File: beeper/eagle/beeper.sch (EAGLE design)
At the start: 32 parts, among them J4 ICSP, Q1 16MHz, T1 MMBT3904, U1 ATA6631, U2 ATMEGA328P

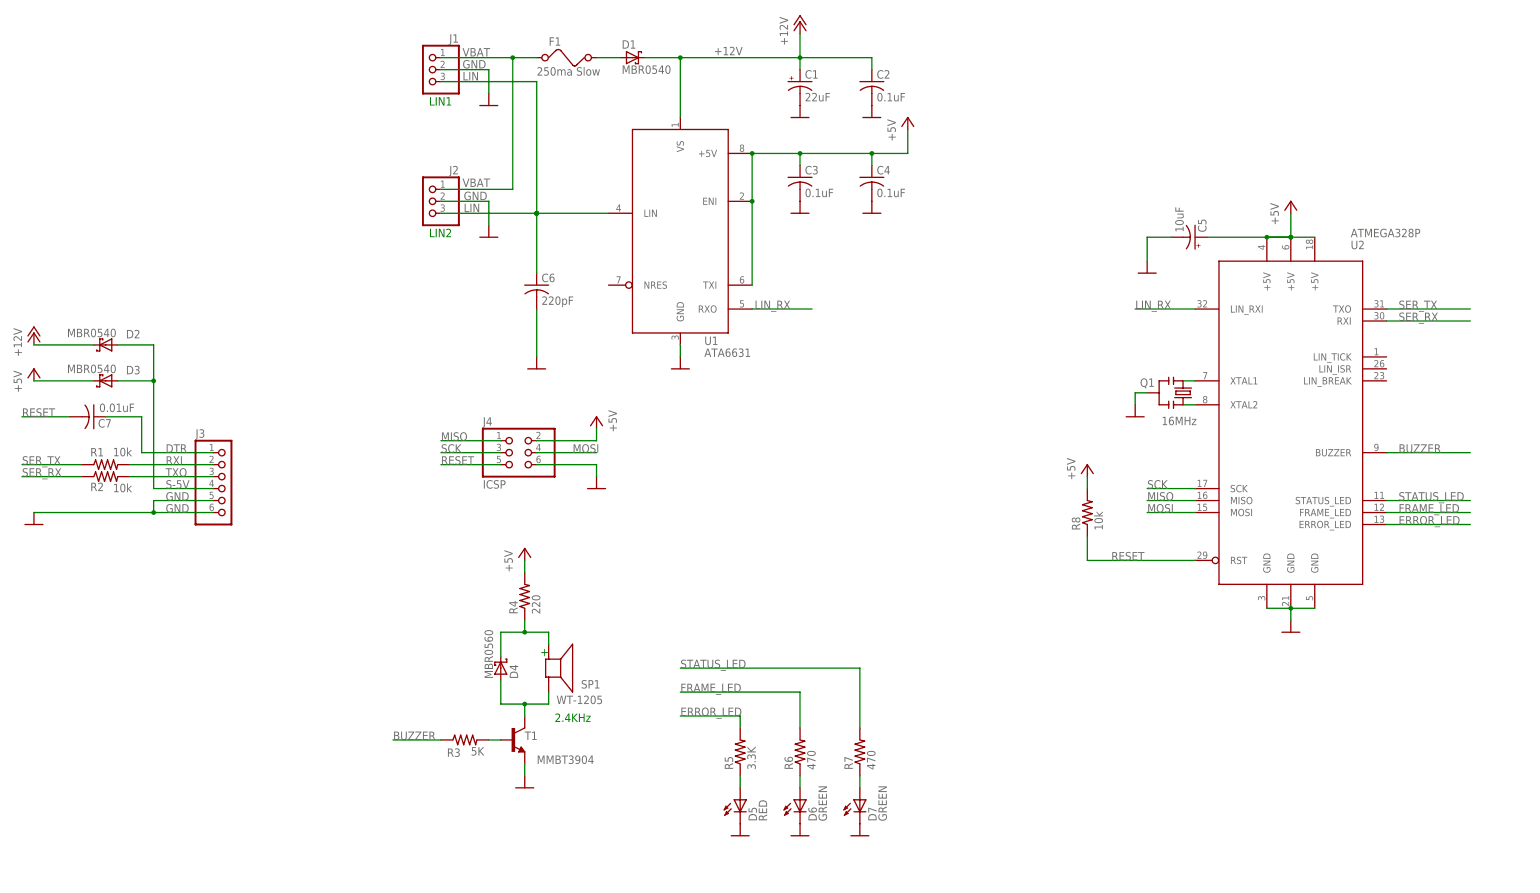
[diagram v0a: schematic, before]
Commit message: Complected the refactoring of the beeper schema. No semantic change.
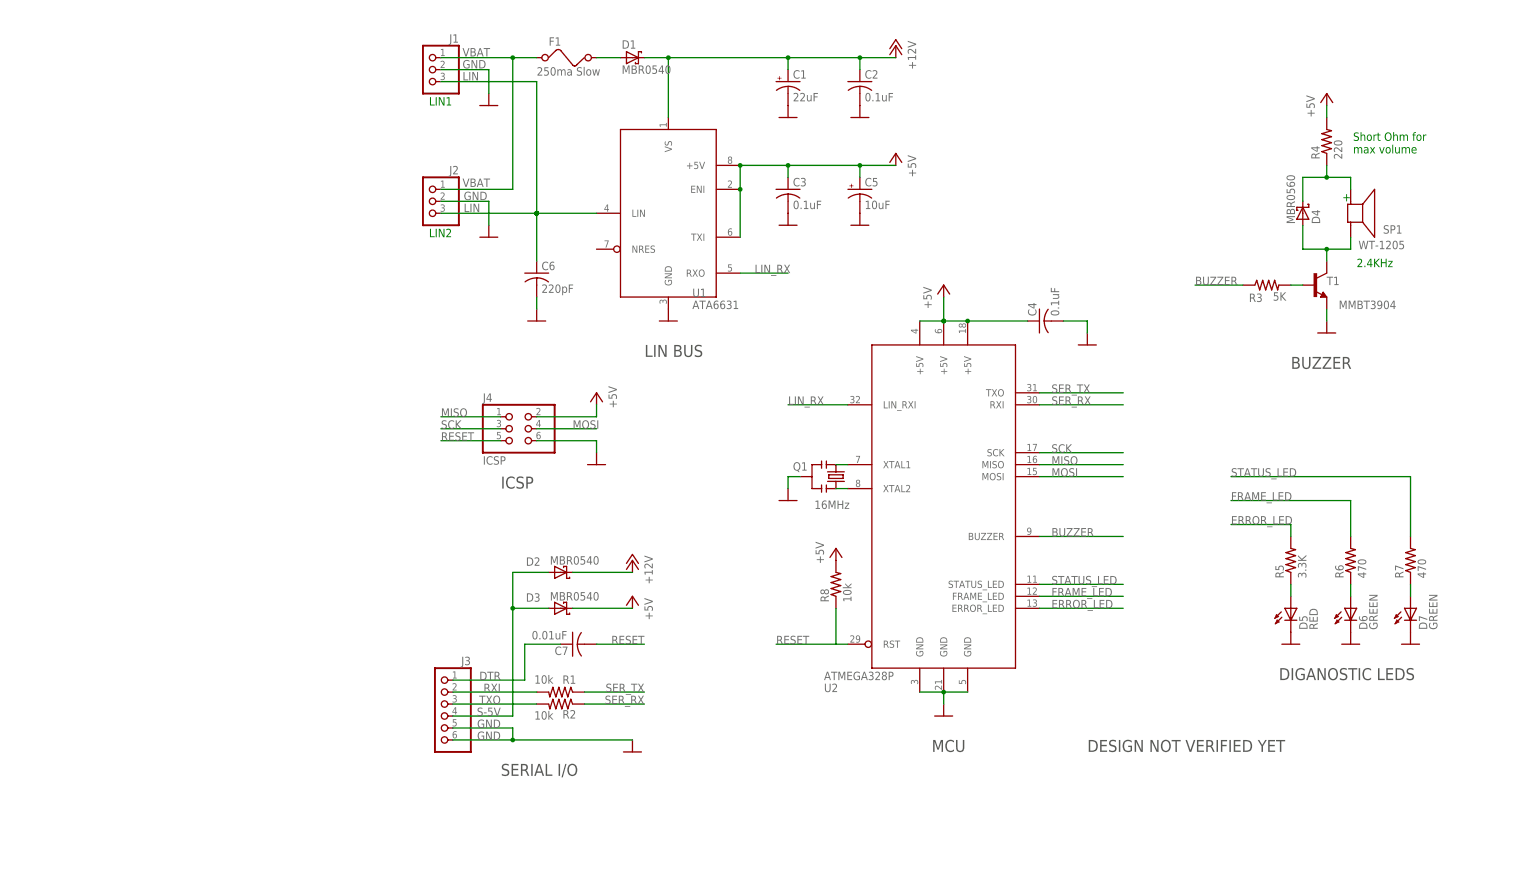
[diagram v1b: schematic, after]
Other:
- note added: "BUZZER"
- note added: "DESIGN NOT VERIFIED YET"
- note added: "DIGANOSTIC LEDS"
- note added: "ICSP"
- note added: "LIN BUS"
- note added: "MCU"
- note added: "SERIAL I/O"
- note added: "Short Ohm for max volume"
- moved on the sheet: C1, C2, C3, C4, C5, C6, C7, D2, D3, D4, D5, D6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

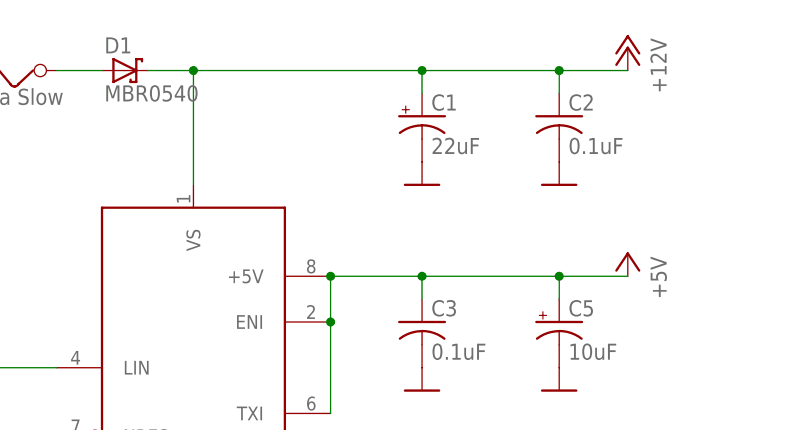
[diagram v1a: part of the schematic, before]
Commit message: Added '40V' annotation to VBAT capacitor.
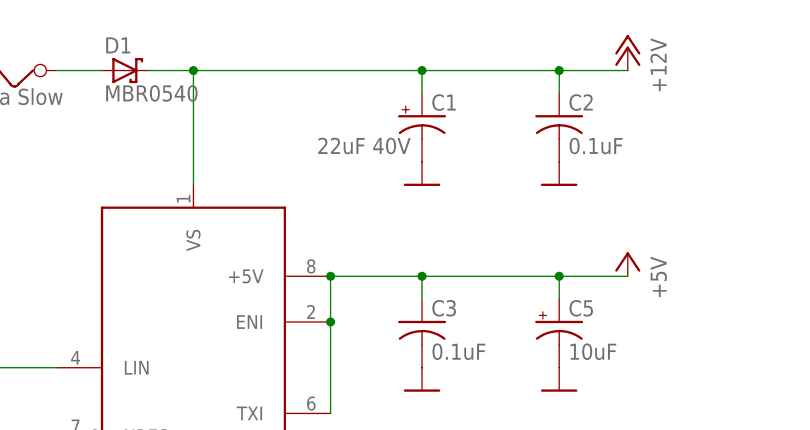
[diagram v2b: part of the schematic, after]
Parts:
- C1: value 22uF -> 22uF 40V
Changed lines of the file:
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@@
 <part name="D6" library="led" deviceset="LED" device="SMT1206" value="GREEN"/>
 <part name="D7" library="led" deviceset="LED" device="SMT1206" value="GREEN"/>
-<part name="C1" library="rcl" deviceset="CPOL-US" device="UD-6,3X5,8" value="22uF"/>
+<part name="C1" library="rcl" deviceset="CPOL-US" device="UD-6,3X5,8" value="22uF 40V"/>
 <part name="C2" library="rcl" deviceset="C-US" device="C0805" value="0.1uF"/>
 <part name="C5" library="rcl" deviceset="CPOL-US" device="A/3216-18R" value="10uF"/>
@@
 <instance part="D6" gate="G$1" x="271.78" y="83.82"/>
 <instance part="D7" gate="G$1" x="284.48" y="83.82"/>
-<instance part="C1" gate="G$1" x="152.4" y="195.58"/>
+<instance part="C1" gate="G$1" x="152.4" y="195.58" smashed="yes">
+<attribute name="NAME" x="153.416" y="196.215" size="1.778" layer="95"/>
+<attribute name="VALUE" x="140.716" y="191.389" size="1.778" layer="96"/>
+</instance>
 <instance part="C2" gate="G$1" x="167.64" y="195.58"/>
 <instance part="C5" gate="G$1" x="167.64" y="172.72"/>

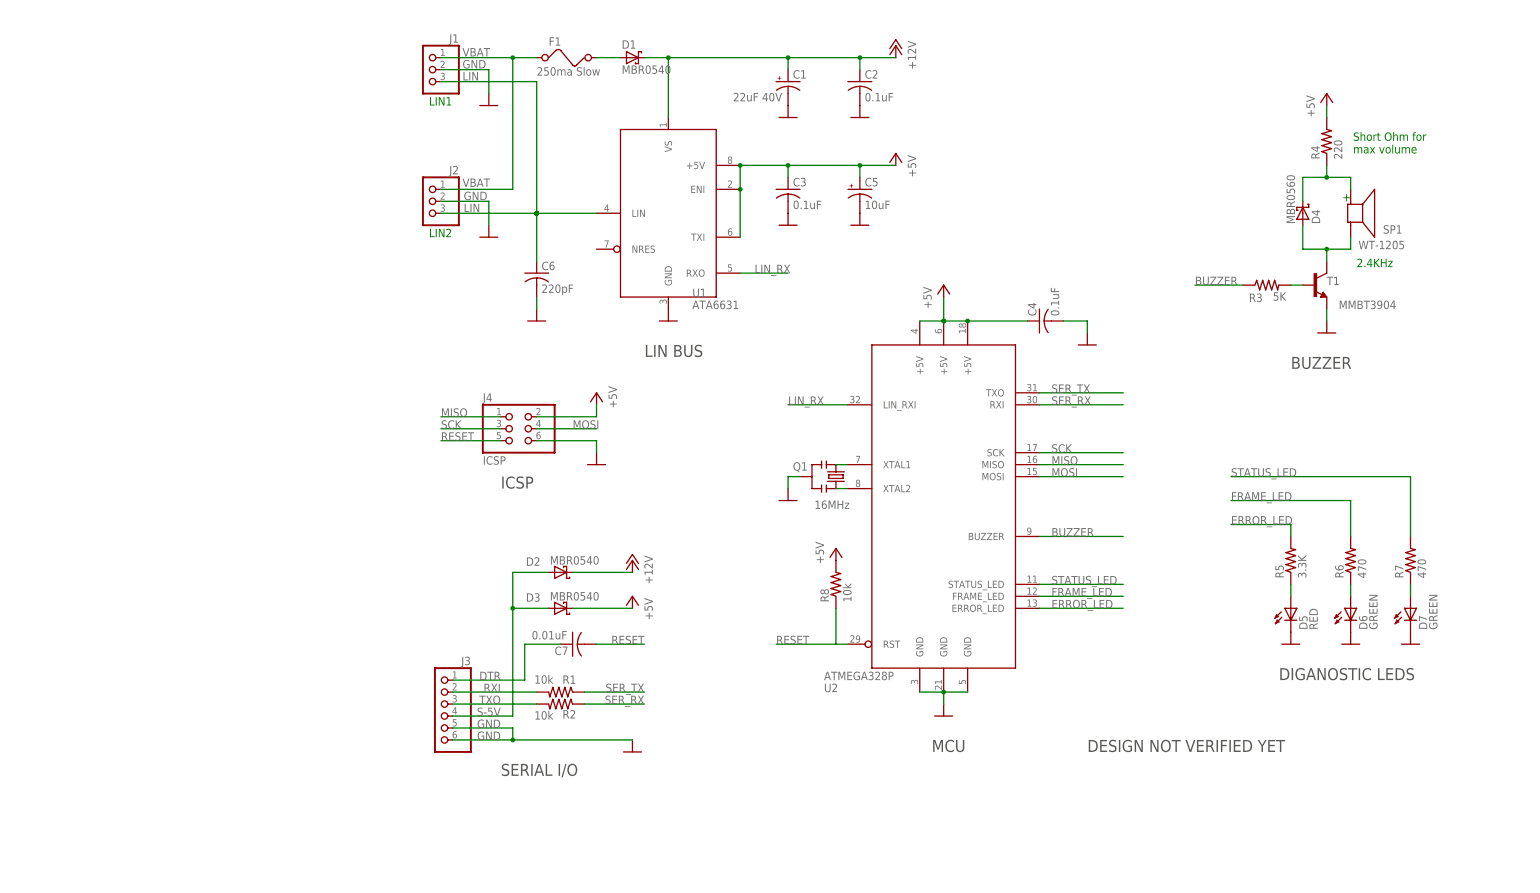
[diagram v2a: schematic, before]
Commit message: Minor text changes in beeper schematic. No semantic change.
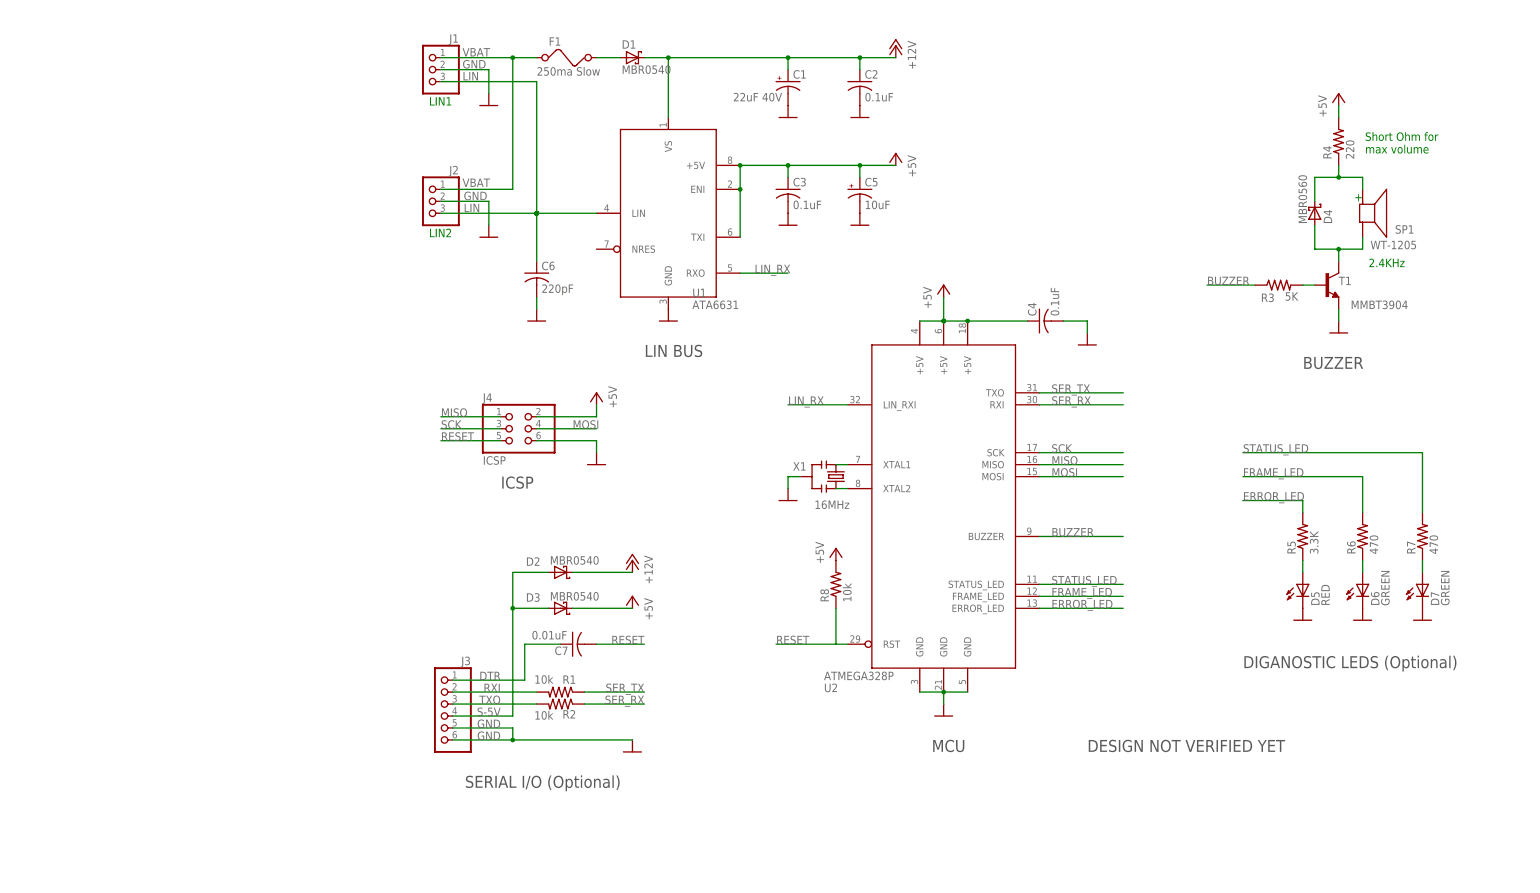
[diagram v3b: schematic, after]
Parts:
- renumbered Q1 to X1
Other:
- note added: "DIGANOSTIC LEDS (Optional)"
- note added: "SERIAL I/O (Optional)"
- note removed: "DIGANOSTIC LEDS"
- note removed: "SERIAL I/O"
- moved on the sheet: D4, D5, D6, D7, R3, R4, R5, R6, R7, SP1, T1

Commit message: Tweaked beeper resistor values. No schema or layout change.
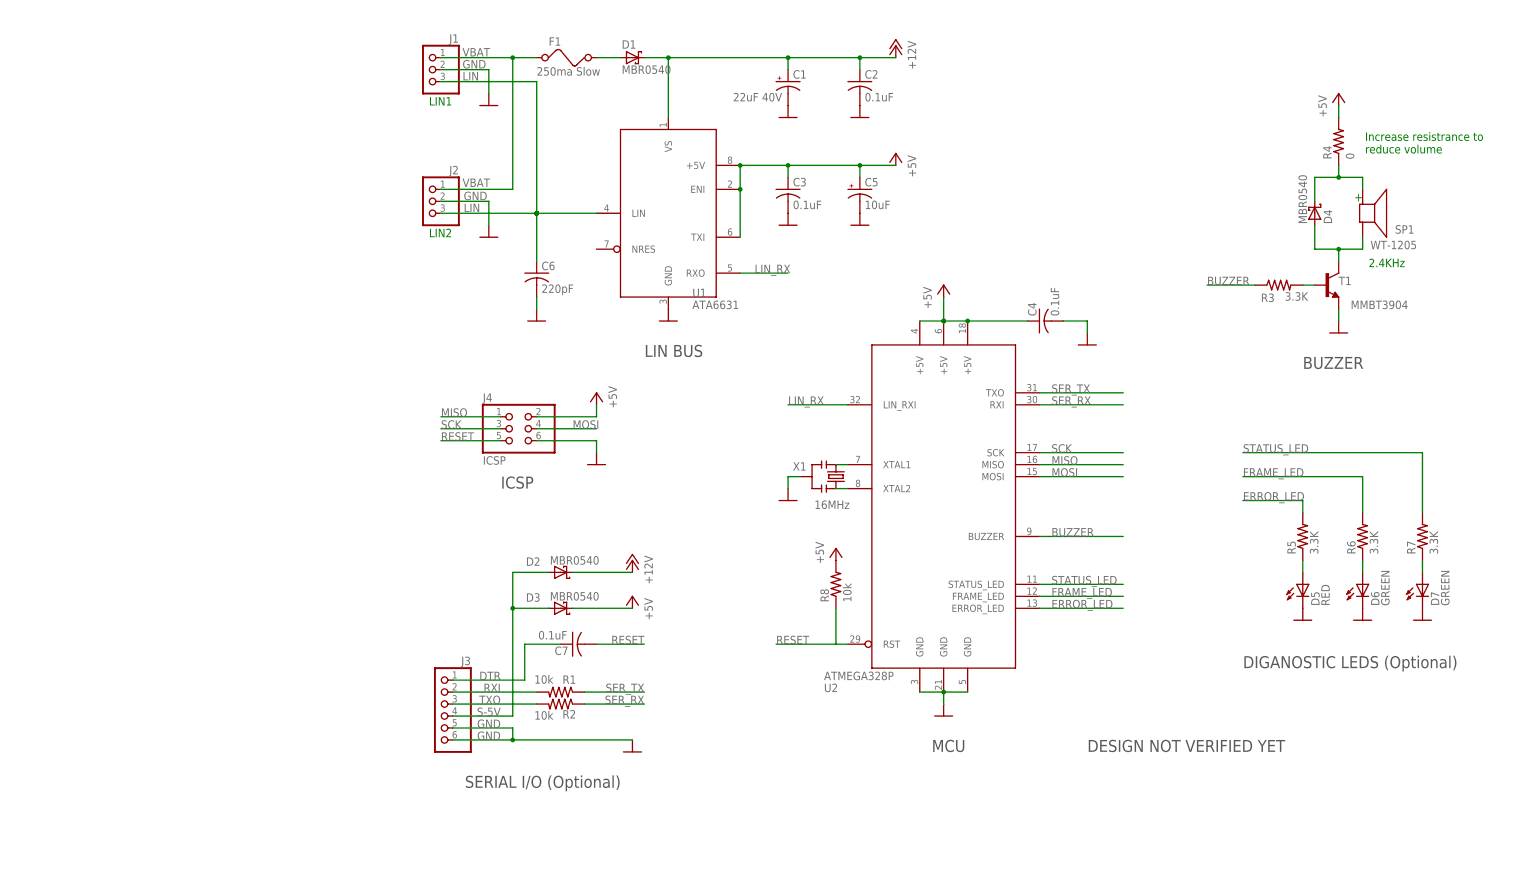
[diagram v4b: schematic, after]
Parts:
- C7: value 0.01uF -> 0.1uF
- D4: value MBR0560 -> MBR0540
- R3: value 5K -> 3.3K
- R4: value 220 -> 0
- R6, R7: value 470 -> 3.3K
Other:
- note added: "Increase resistrance to reduce volume"
- note removed: "Short Ohm for max volume"
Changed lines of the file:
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@@
 <parts>
 <part name="R5" library="rcl" deviceset="R-US_" device="R0805" value="3.3K"/>
-<part name="R6" library="rcl" deviceset="R-US_" device="R0805" value="470"/>
-<part name="R7" library="rcl" deviceset="R-US_" device="R0805" value="470"/>
+<part name="R6" library="rcl" deviceset="R-US_" device="R0805" value="3.3K"/>
+<part name="R7" library="rcl" deviceset="R-US_" device="R0805" value="3.3K"/>
 <part name="C6" library="rcl" deviceset="C-US" device="C0805" value="220pF"/>
 <part name="J1" library="pinhead" deviceset="PINHD-1X3" device=""/>
@@
 <part name="C3" library="rcl" deviceset="C-US" device="C0805" value="0.1uF"/>
 <part name="GND12" library="beeper" deviceset="GND" device=""/>
-<part name="C7" library="rcl" deviceset="C-US" device="C0805" value="0.01uF"/>
+<part name="C7" library="rcl" deviceset="C-US" device="C0805" value="0.1uF"/>
 <part name="P+2" library="supply1" deviceset="+5V" device=""/>
 <part name="R1" library="rcl" deviceset="R-US_" device="R0805" value="10k"/>
@@
 <part name="GND14" library="beeper" deviceset="GND" device=""/>
 <part name="P+5" library="supply1" deviceset="+5V" device=""/>
-<part name="R3" library="rcl" deviceset="R-US_" device="R0805" value="5K"/>
+<part name="R3" library="rcl" deviceset="R-US_" device="R0805" value="3.3K"/>
 <part name="T1" library="transistor" deviceset="*-NPN-" device="SOT23-BEC" technology="MMBT3904LT1" value="MMBT3904"/>
 <part name="GND18" library="beeper" deviceset="GND" device=""/>
 <part name="P+3" library="supply1" deviceset="+5V" device=""/>
-<part name="R4" library="rcl" deviceset="R-US_" device="R0805" value="220"/>
+<part name="R4" library="rcl" deviceset="R-US_" device="R0805" value="0"/>
 <part name="R8" library="rcl" deviceset="R-US_" device="R0805" value="10k"/>
 <part name="P+6" library="supply1" deviceset="+5V" device=""/>
@@
 <part name="GND8" library="beeper" deviceset="GND" device=""/>
 <part name="SP1" library="beeper" deviceset="AL60P" device="" value="WT-1205"/>
-<part name="D4" library="diode" deviceset="SMF5.0AT1" device="" value="MBR0560"/>
+<part name="D4" library="diode" deviceset="SMF5.0AT1" device="" value="MBR0540"/>
 <part name="D5" library="led" deviceset="LED" device="SMT1206" value="RED"/>
 <part name="D6" library="led" deviceset="LED" device="SMT1206" value="GREEN"/>
@@
 <text x="261.62" y="134.62" size="2.54" layer="97">BUZZER</text>
 <text x="215.9" y="53.34" size="2.54" layer="97">DESIGN NOT VERIFIED YET</text>
-<text x="274.828" y="180.34" size="1.778" layer="91">Short Ohm for
-max volume</text>
+<text x="274.828" y="180.34" size="1.778" layer="91">Increase resistrance to
+reduce volume</text>
 </plain>
 <instances>
